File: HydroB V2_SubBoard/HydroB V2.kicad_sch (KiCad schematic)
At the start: 0 parts

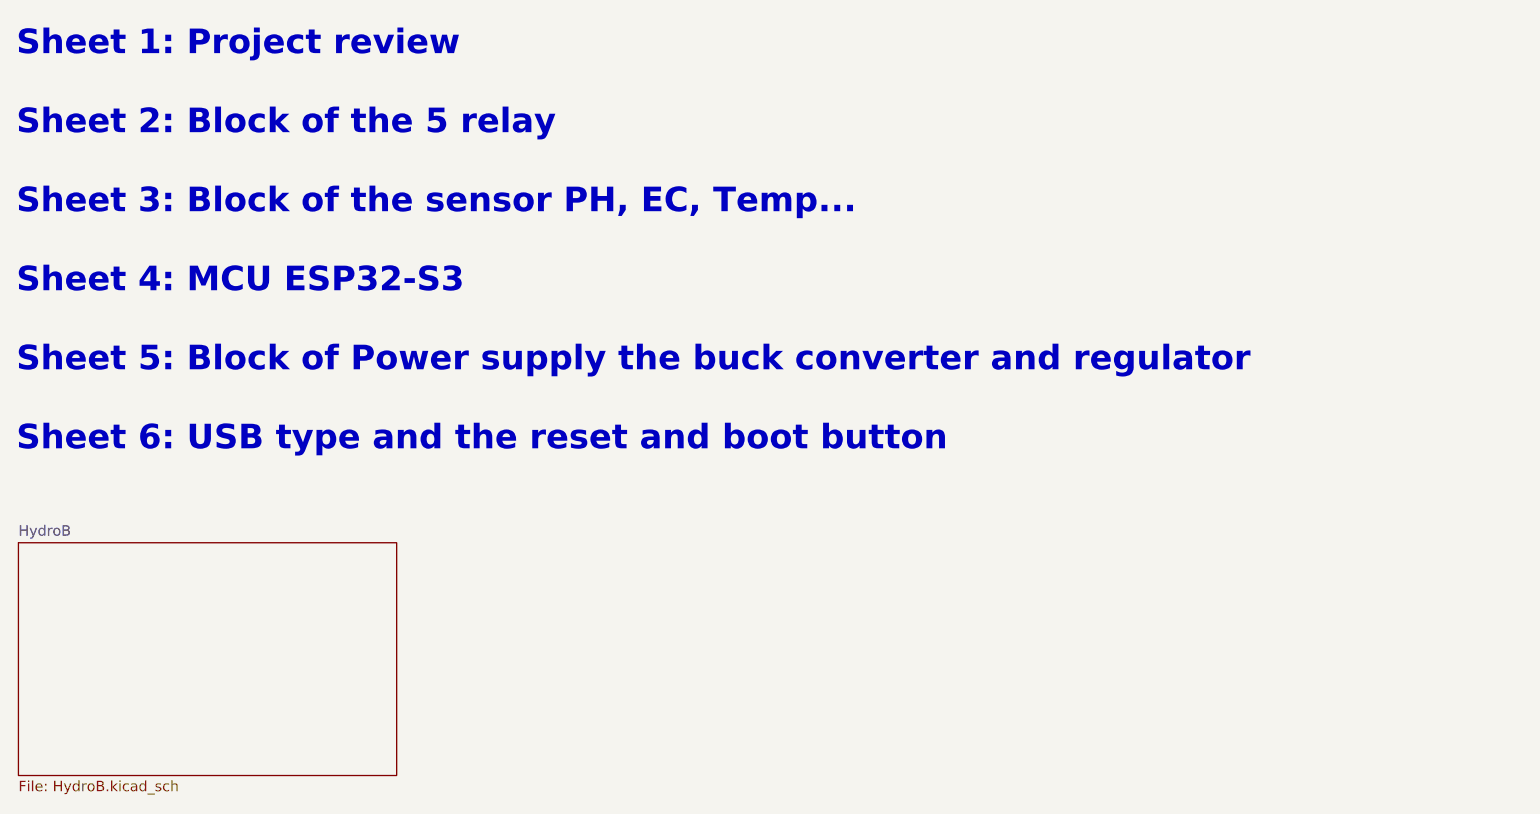
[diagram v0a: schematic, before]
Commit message: the schematic of sub-board updated
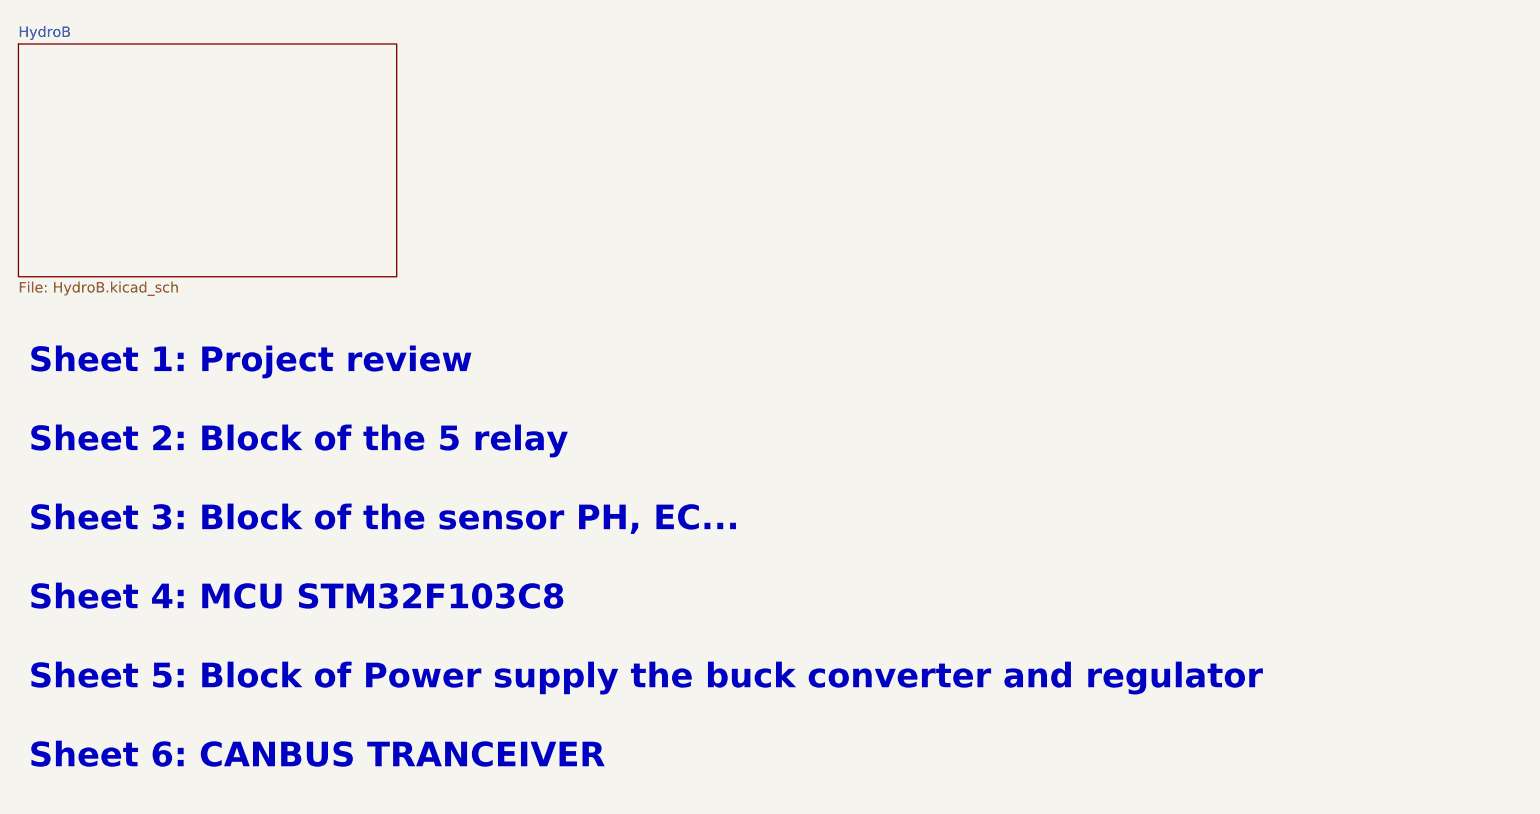
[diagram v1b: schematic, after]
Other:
- note added: "Sheet 1: Project review Sheet 2: Block of the 5 relay Sheet 3: Block of the sensor PH, EC... Sheet 4: MCU STM32F103C8 Sheet 5: Block of Power supply the buck converter and regulator Sheet 6: CANBUS TRANCEIVER"
- note removed: "Sheet 1: Project review Sheet 2: Block of the 5 relay Sheet 3: Block of the sensor PH, EC, Temp... Sheet 4: MCU ESP32-S3 Sheet 5: Block of Power supply the buck converter and regulator Sheet 6: USB type and the reset and boot button"
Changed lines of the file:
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@@
 	(generator_version "8.0")
 	(paper "A4")
-	(text "Sheet 1: Project review \n\nSheet 2: Block of the 5 relay\n\nSheet 3: Block of the sensor PH, EC, Temp...\n\nSheet 4: MCU ESP32-S3\n\nSheet 5: Block of Power supply the buck converter and regulator\n\nSheet 6: USB type and the reset and boot button"
+	(text "Sheet 1: Project review \n\nSheet 2: Block of the 5 relay\n\nSheet 3: Block of the sensor PH, EC...\n\nSheet 4: MCU STM32F103C8\n\nSheet 5: Block of Power supply the buck converter and regulator\n\nSheet 6: CANBUS TRANCEIVER\n"
 		(exclude_from_sim no)
-		(at 17.526 18.034 0)
+		(at 19.05 56.896 0)
 		(effects
 			(font
@@
 	)
 	(sheet
-		(at 17.78 80.772)
+		(at 17.78 19.812)
 		(size 46.228 28.448)
 		(fields_autoplaced yes)
@@
 		)
 		(property "Sheetname" "HydroB"
-			(at 17.78 80.0604 0)
+			(at 17.78 19.1004 0)
 			(effects
 				(font
@@
 		)
 		(property "Sheetfile" "HydroB.kicad_sch"
-			(at 17.78 109.8046 0)
+			(at 17.78 48.8446 0)
 			(effects
 				(font
